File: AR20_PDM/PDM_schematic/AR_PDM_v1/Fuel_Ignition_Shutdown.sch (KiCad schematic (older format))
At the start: 28 parts, among them K1 DIPxx-1Cxx-51x, K2 DIPxx-1Cxx-51x, U11 N-MOS, U12 P-MOS, U13 N-MOS, U14 N-MOS, U29 INA233, U30 INA233

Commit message: Working on pcb layout
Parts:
- removed D? (x2): D_Schottky_x2, symbol AR20_PDM_v1-rescue:D_Schottky_x2
- added D48, D50: DIODE, Diode_THT:D_5W_P10.16mm_Horizontal, symbol AR20_PDM_v1-rescue:DIODE-CustomSymbol
- added D57, D58, D59, D60: D_Schottky_BAT60A, AR_PDM_v1:D_Shotky_BAT60_HandSoldering, symbol AR20_PDM_v1-rescue:D_Schottky_BAT60A
- D30, D31: footprint AR_PDM_v1:SODFL2512X73N -> AR_PDM_v1:Diode-SODFL2512X73N
- gave numbers to parts that had none: 4
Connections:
- wire segments 123 -> 136
- no-connect marks 2 -> 4
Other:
- moved on the sheet: JP1

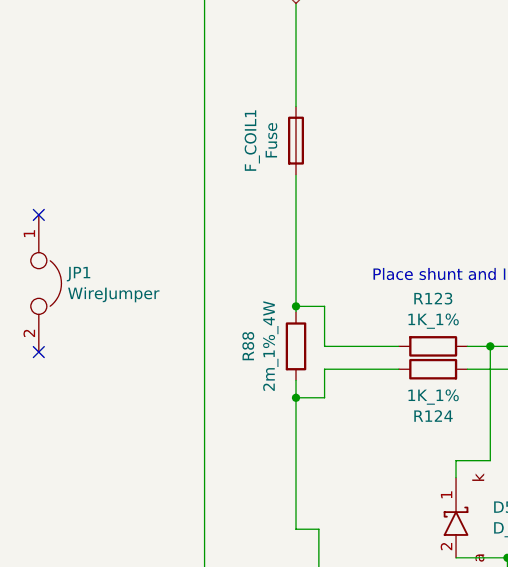
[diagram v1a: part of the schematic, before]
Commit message: PDM mostly complete
- Reverse polarity protection implemented
- All traces layed out
- final polish missing
- DRC missing
- Final check missing
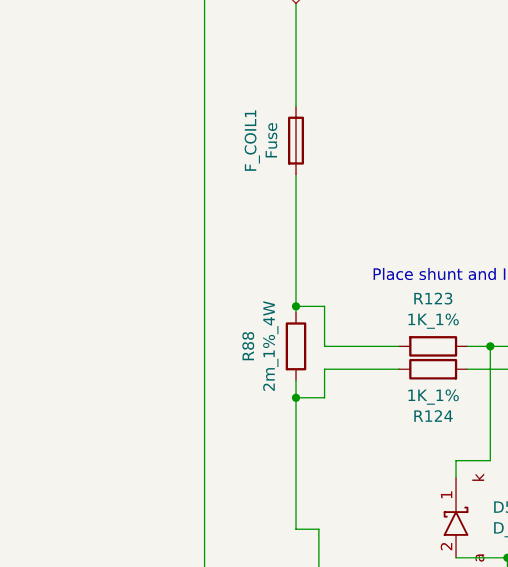
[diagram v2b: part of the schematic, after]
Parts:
- removed JP1: WireJumper, AR_PDM_v1:WireJumper_12mm, symbol Device:Jumper
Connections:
- no-connect marks 4 -> 2
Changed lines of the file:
@@
 Wire Wire Line
 	8700 2150 8700 2450
-$Comp
-L Device:Jumper JP1
-U 1 1 5E8039E3
-P 825 4425
-F 0 "JP1" V 779 4551 50  0000 L CNN
-F 1 "WireJumper" V 870 4551 50  0000 L CNN
-F 2 "AR_PDM_v1:WireJumper_12mm" H 825 4425 50  0001 C CNN
-F 3 "~" H 825 4425 50  0001 C CNN
-	1    825  4425
-	0    1    1    0
-$EndComp
 Connection ~ 6600 4300
 Wire Wire Line
@@
 Wire Wire Line
 	6600 4300 6600 5375
-NoConn ~ 825  4125
-NoConn ~ 825  4725
 $Comp
 L AR20_PDM_v1-rescue:D_Schottky_BAT60A D?

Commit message: Mostly finalized
- Fixed alot of the masking
- Replaced main Flyback diodes to shotky type with low VF
- Fix DRC one footprint still to small clearance
- Fix silkscreen
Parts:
- D48, D50: footprint Diode_THT:D_5W_P10.16mm_Horizontal -> Diode_SMD:D_SMB_Handsoldering
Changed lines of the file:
@@
 F 0 "D50" V 7704 4430 50  0000 L CNN
 F 1 "DIODE" V 7795 4430 50  0000 L CNN
-F 2 "Diode_THT:D_5W_P10.16mm_Horizontal" H 7750 4350 50  0001 C CNN
+F 2 "Diode_SMD:D_SMB_Handsoldering" H 7750 4350 50  0001 C CNN
 F 3 "" H 7750 4350 50  0001 C CNN
 F 4 "Y" H 7750 4350 50  0001 L CNN "Spice_Netlist_Enabled"
@@
 F 0 "D48" V 2354 6580 50  0000 L CNN
 F 1 "DIODE" V 2445 6580 50  0000 L CNN
-F 2 "Diode_THT:D_5W_P10.16mm_Horizontal" H 2400 6500 50  0001 C CNN
+F 2 "Diode_SMD:D_SMB_Handsoldering" H 2400 6500 50  0001 C CNN
 F 3 "" H 2400 6500 50  0001 C CNN
 F 4 "Y" H 2400 6500 50  0001 L CNN "Spice_Netlist_Enabled"

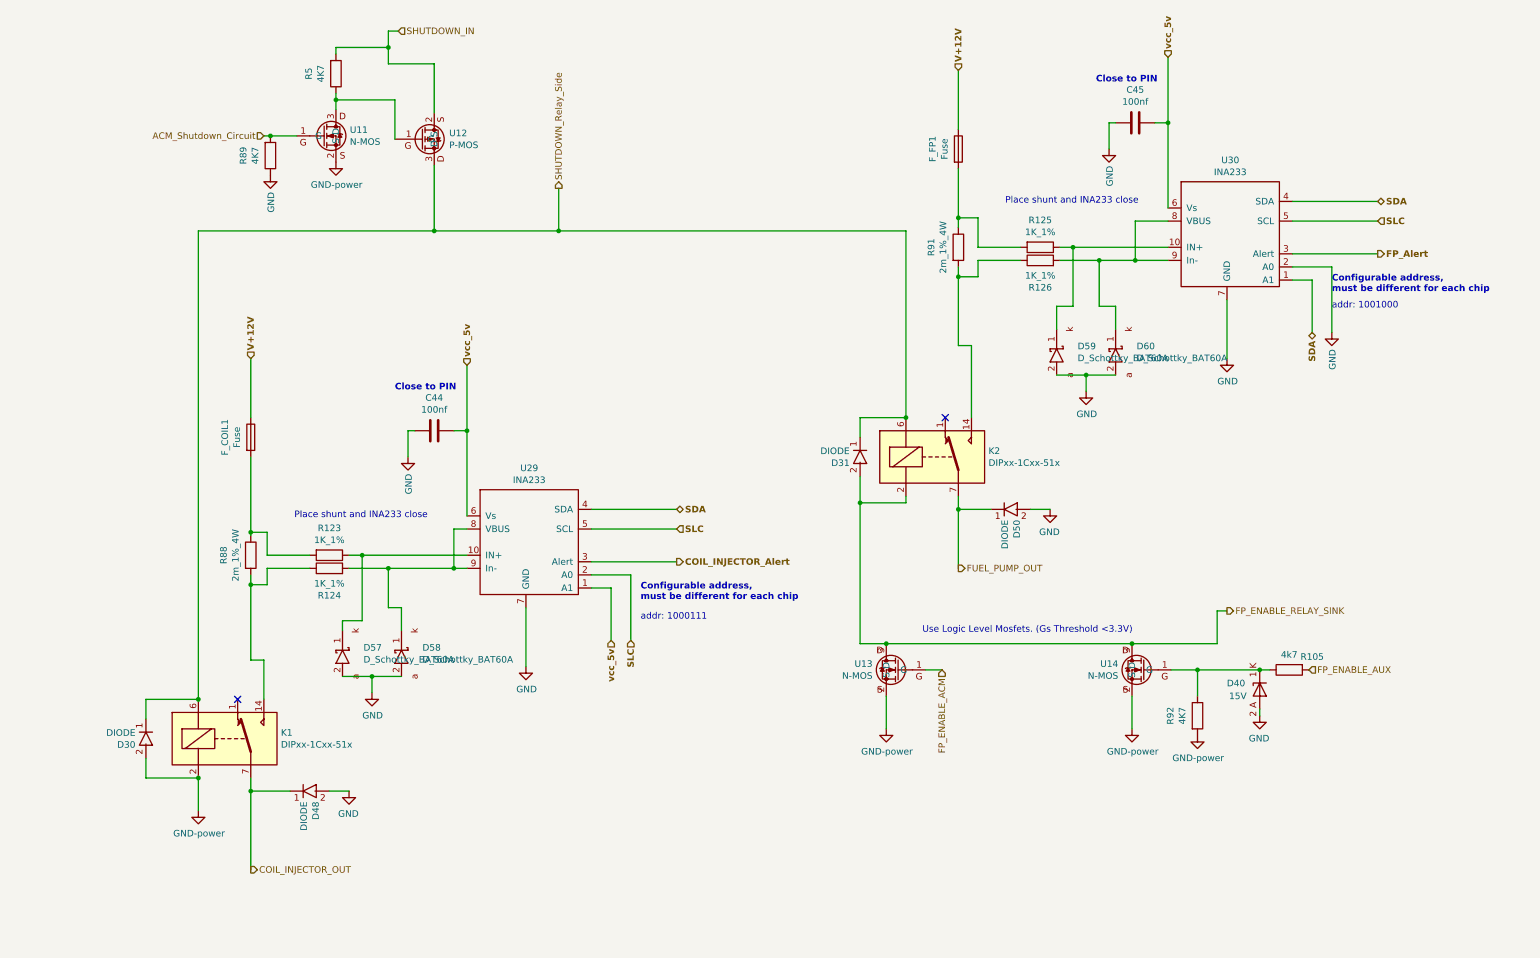
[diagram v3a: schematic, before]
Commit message: shematics adjustments, and fixing values and names
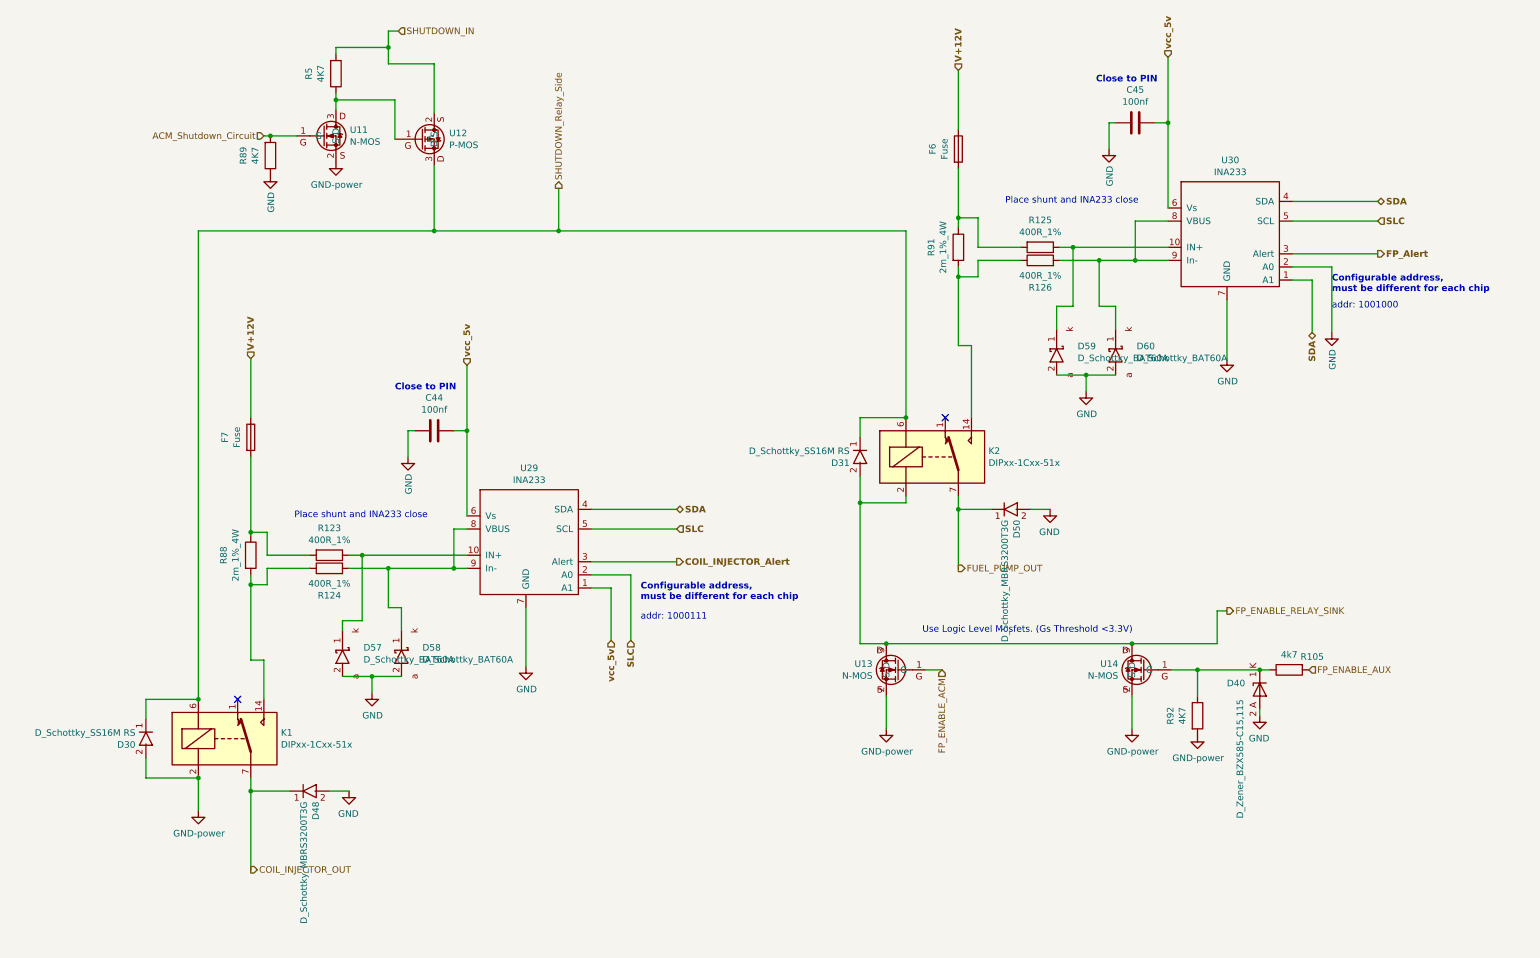
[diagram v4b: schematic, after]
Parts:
- D30, D31: value DIODE -> D_Schottky_SS16M RS
- D40: value 15V -> D_Zener_BZX585-C15,115
- D48, D50: value DIODE -> D_Schottky_MBRS3200T3G
- R123, R124, R125, R126: value 1K_1% -> 400R_1%
- renumbered F_FP1 to F6, F_COIL1 to F7
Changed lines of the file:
@@
 P 6600 3950
 F 0 "D31" V 6554 4030 50  0000 L CNN
-F 1 "DIODE" V 6645 4030 50  0000 L CNN
+F 1 "D_Schottky_SS16M RS" V 6645 4030 50  0000 L CNN
 F 2 "AR_PDM_v1:Diode-SODFL2512X73N" H 6600 3950 50  0001 C CNN
 F 3 "" H 6600 3950 50  0001 C CNN
@@
 COIL_INJECTOR_OUT
 $Comp
-L Device:Fuse F_FP1
+L Device:Fuse F6
 U 1 1 5DDF15AA
 P 7350 1600
-F 0 "F_FP1" V 7153 1600 50  0000 C CNN
+F 0 "F6" V 7153 1600 50  0000 C CNN
 F 1 "Fuse" V 7244 1600 50  0000 C CNN
 F 2 "AR_PDM_v1:FuseHolder" V 7280 1600 50  0001 C CNN
@@
 P 1150 6100
 F 0 "D30" V 1104 6180 50  0000 L CNN
-F 1 "DIODE" V 1195 6180 50  0000 L CNN
+F 1 "D_Schottky_SS16M RS" V 1195 6180 50  0000 L CNN
 F 2 "AR_PDM_v1:Diode-SODFL2512X73N" H 1150 6100 50  0001 C CNN
 F 3 "" H 1150 6100 50  0001 C CNN
@@
 	7350 1450 7350 1000
 $Comp
-L Device:Fuse F_COIL1
+L Device:Fuse F7
 U 1 1 5DE5EBA7
 P 1950 3800
-F 0 "F_COIL1" V 1753 3800 50  0000 C CNN
+F 0 "F7" V 1753 3800 50  0000 C CNN
 F 1 "Fuse" V 1844 3800 50  0000 C CNN
 F 2 "AR_PDM_v1:FuseHolder" V 1880 3800 50  0001 C CNN
@@
 AR Path="/5DA8920B/5EEF3E55" Ref="R125"  Part="1"
 F 0 "R125" V 7768 2350 50  0000 C CNN
-F 1 "1K_1%" V 7859 2350 50  0000 C CNN
+F 1 "400R_1%" V 7859 2350 50  0000 C CNN
 F 2 "Resistor_SMD:R_0603_1608Metric" V 7905 2350 50  0001 C CNN
 F 3 "~" H 7975 2350 50  0001 C CNN
@@
 AR Path="/5DA8920B/5EEF3E5E" Ref="R126"  Part="1"
 F 0 "R126" V 7768 2450 50  0000 C CNN
-F 1 "1K_1%" V 7859 2450 50  0000 C CNN
+F 1 "400R_1%" V 7859 2450 50  0000 C CNN
 F 2 "Resistor_SMD:R_0603_1608Metric" V 7905 2450 50  0001 C CNN
 F 3 "~" H 7975 2450 50  0001 C CNN
@@
 AR Path="/5DA8920B/5EF32931" Ref="R123"  Part="1"
 F 0 "R123" V 2343 4700 50  0000 C CNN
-F 1 "1K_1%" V 2434 4700 50  0000 C CNN
+F 1 "400R_1%" V 2434 4700 50  0000 C CNN
 F 2 "Resistor_SMD:R_0603_1608Metric" V 2480 4700 50  0001 C CNN
 F 3 "~" H 2550 4700 50  0001 C CNN
@@
 AR Path="/5DA8920B/5EF32937" Ref="R124"  Part="1"
 F 0 "R124" V 2343 4800 50  0000 C CNN
-F 1 "1K_1%" V 2434 4800 50  0000 C CNN
+F 1 "400R_1%" V 2434 4800 50  0000 C CNN
 F 2 "Resistor_SMD:R_0603_1608Metric" V 2480 4800 50  0001 C CNN
 F 3 "~" H 2550 4800 50  0001 C CNN
@@
 P 7750 4350
 F 0 "D50" V 7704 4430 50  0000 L CNN
-F 1 "DIODE" V 7795 4430 50  0000 L CNN
+F 1 "D_Schottky_MBRS3200T3G" V 7795 4430 50  0000 L CNN
 F 2 "Diode_SMD:D_SMB_Handsoldering" H 7750 4350 50  0001 C CNN
 F 3 "" H 7750 4350 50  0001 C CNN
@@
 P 2400 6500
 F 0 "D48" V 2354 6580 50  0000 L CNN
-F 1 "DIODE" V 2445 6580 50  0000 L CNN
+F 1 "D_Schottky_MBRS3200T3G" V 2445 6580 50  0000 L CNN
 F 2 "Diode_SMD:D_SMB_Handsoldering" H 2400 6500 50  0001 C CNN
 F 3 "" H 2400 6500 50  0001 C CNN
@@
 AR Path="/5DA8920B/5E718482" Ref="D40"  Part="1"
 F 0 "D40" V 9602 5836 50  0000 L CNN
-F 1 "15V" V 9700 5825 50  0000 L CNN
+F 1 "D_Zener_BZX585-C15,115" H 9725 5875 50  0000 L CNN
 F 2 "AR_PDM_v1:Diode-BZX585-C15,115" H 9650 5725 50  0001 C CNN
 F 3 "" H 9650 5725 50  0001 C CNN
